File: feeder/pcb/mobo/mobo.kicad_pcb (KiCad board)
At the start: 2 copper layers, 200 x 100 mm, 66 parts, among them J1 FTDI_HEADER, J2 PLATED_PADS, J3 SWD_10, M1 DRIVE_MOTOR, M2 PEEL_MOTOR, SW1 BUTTON_1, SW2 BUTTON_2, SW3 RESET, U1 TCS40DPR, U2 VCNT2020, U3 MAX3078E, U4 DRV8833PWP, U5 AP1117-33, U6 STM32F103C8Tx, U7 MCP16301, U8 QRE1113, Y1 8MHz

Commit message: Fixes #253
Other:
- rule pad_to_mask_clearance: 0.04 -> 0

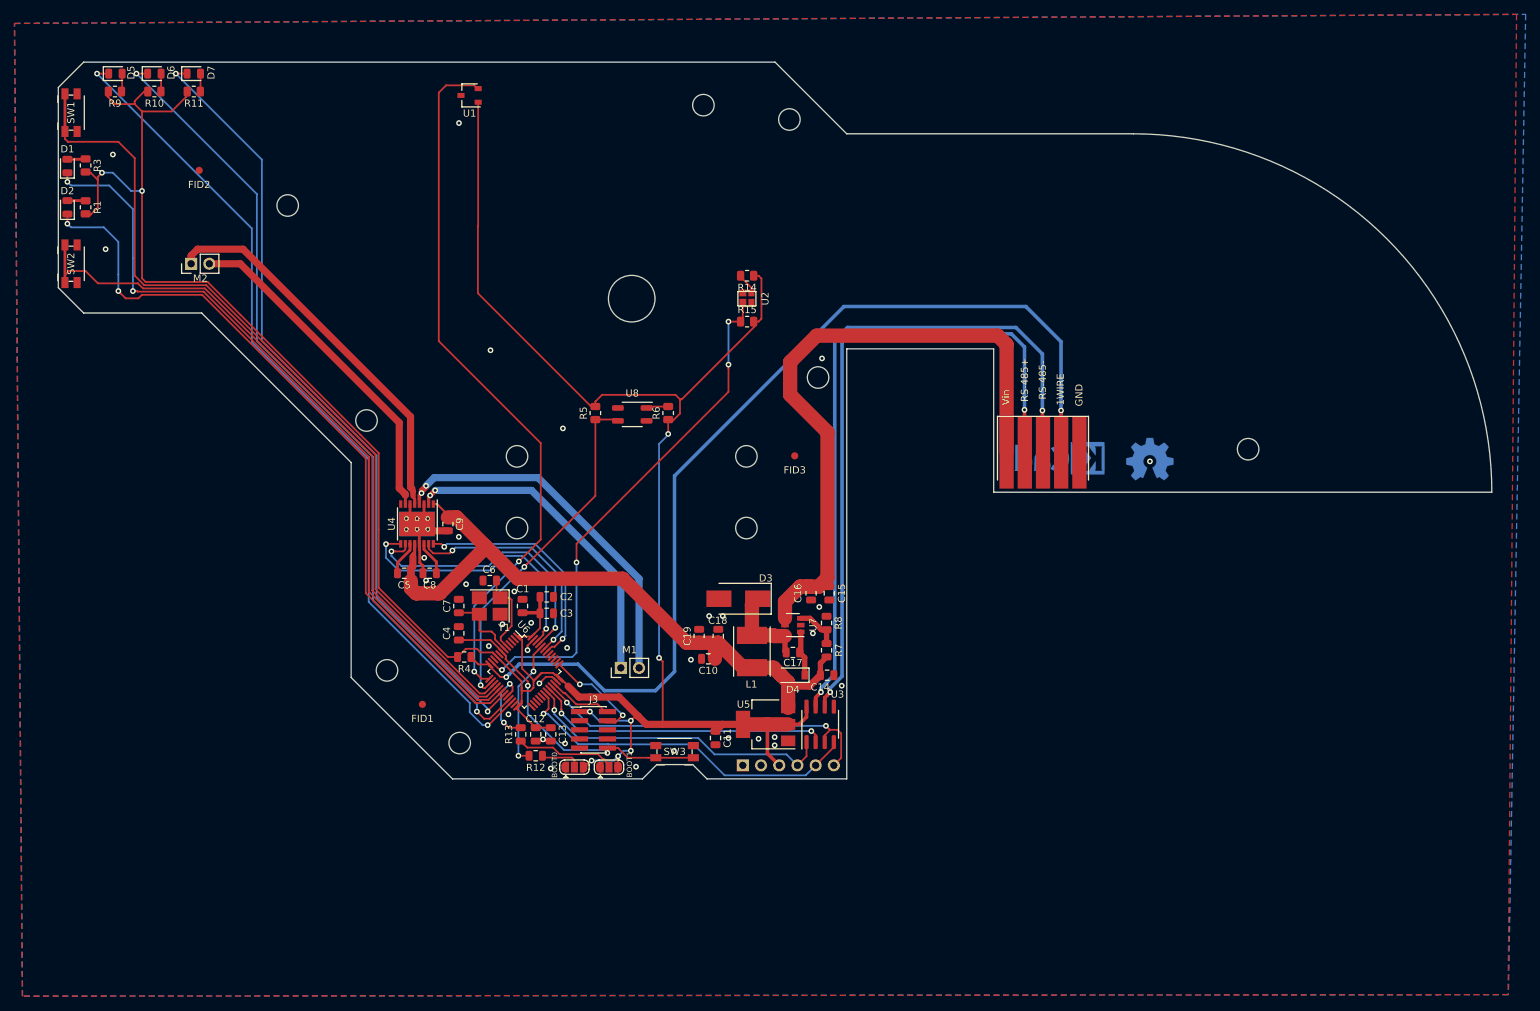
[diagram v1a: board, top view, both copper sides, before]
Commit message: Cleanup Feeders and beautify them
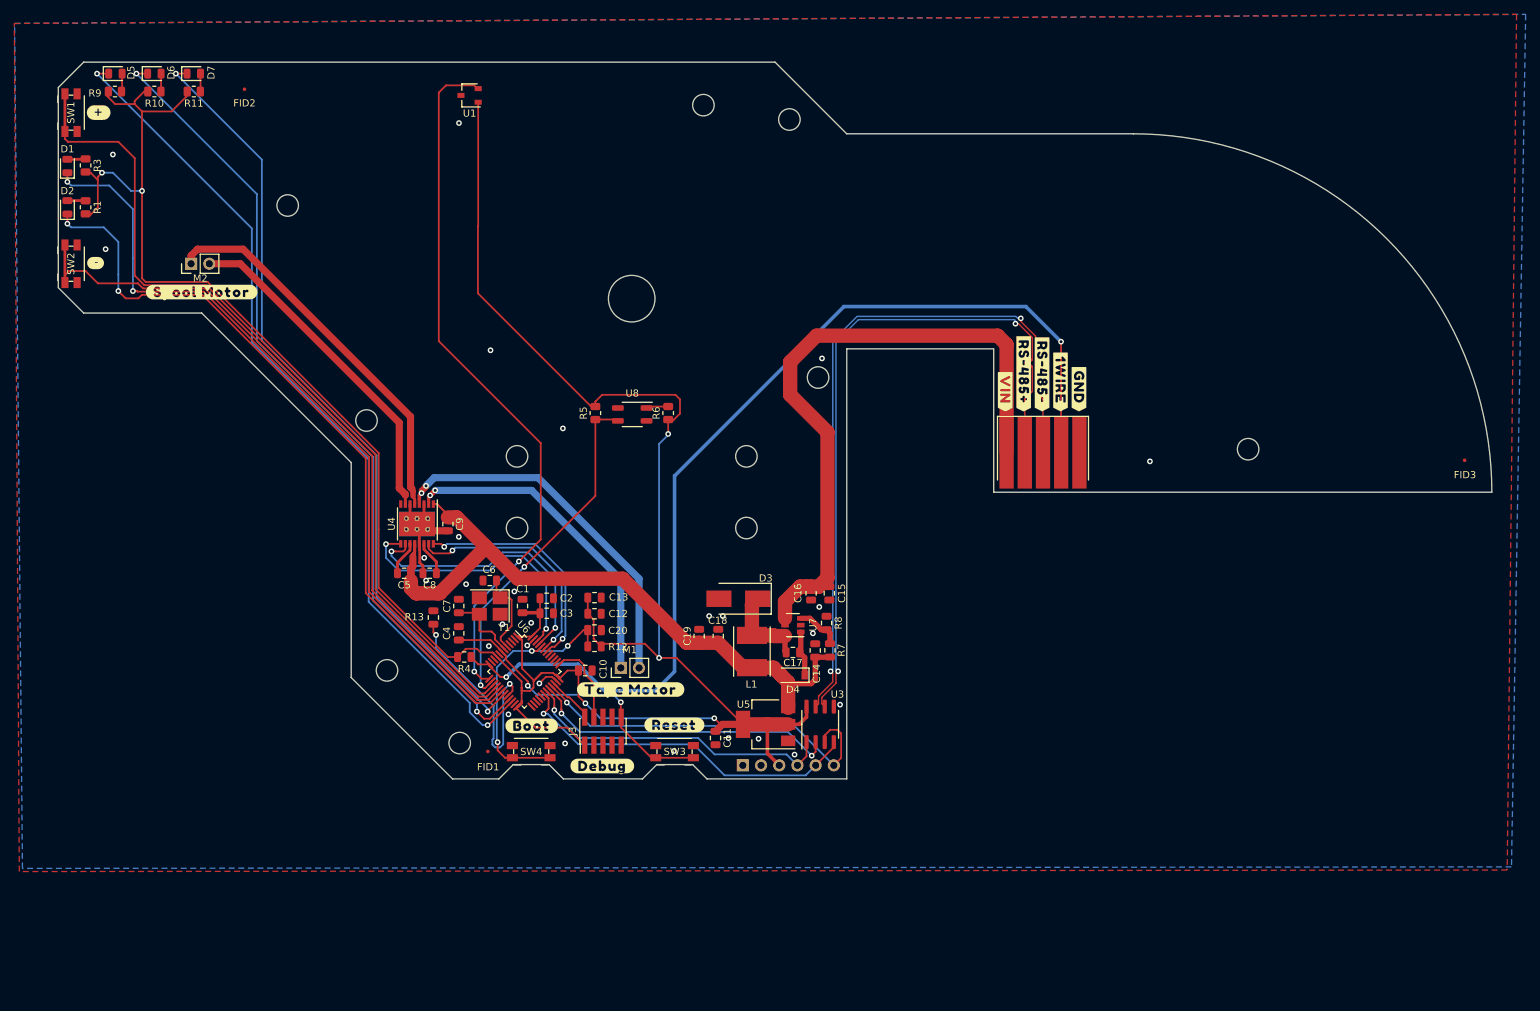
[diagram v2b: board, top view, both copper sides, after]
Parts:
- removed JP2, JP3: SolderJumper_3_Open, Jumper:SolderJumper-3_P1.3mm_Open_RoundedPad1.0x1.5mm
- removed R14: 470R, Resistor_SMD:R_0805_2012Metric
- removed R15: 10K, Resistor_SMD:R_0805_2012Metric
- removed REF**: OSHW-Symbol_6.7x6mm_Copper, Symbol:OSHW-Symbol_6.7x6mm_Copper
- removed REF**: KiCad-Logo_5mm_Copper, Symbol:KiCad-Logo_5mm_Copper
- removed U2: VCNT2020, index:VCNT2020
- added ?: , buzzard_labels, B.Cu at (8.57, 12.4)
- added ?: , buzzard_labels, B.Cu at (184.2, 57.6)
- added ?: , buzzard_labels, F.Cu at (148.5, 50.8)
- added ?: , buzzard_labels, F.Cu at (145.9, 49.8)
- added ?: , buzzard_labels, F.Cu at (143.4, 48.7)
- added ?: , buzzard_labels, F.Cu at (140.8, 48.6)
- added ?: , buzzard_labels, F.Cu at (138.2, 51.1)
- added ?: , buzzard_labels, B.Cu at (114.4, 99.0)
- added ?: , buzzard_labels, B.Cu at (111.8, 98.8)
- added ?: , buzzard_labels, B.Cu at (109.2, 98.9)
- added ?: , buzzard_labels, B.Cu at (106.7, 97.8)
- added ?: , buzzard_labels, B.Cu at (7.85, 33.5)
- added ?: , buzzard_labels, B.Cu at (104.1, 98.9)
- added ?: , buzzard_labels, B.Cu at (101.6, 98.1)
- added ?: , buzzard_labels, B.Cu at (92.1, 101.7)
- added ?: , buzzard_labels, B.Cu at (72.1, 101.7)
- added ?: , buzzard_labels, F.Cu at (72.1, 98.0)
- added ?: , buzzard_labels, F.Cu at (92.0, 97.9)
- added ?: , buzzard_labels, F.Cu at (11.3, 33.4)
- added ?: , buzzard_labels, F.Cu at (11.7, 12.4)
- added ?: , buzzard_labels, F.Cu at (26.1, 37.5)
- added ?: , buzzard_labels, F.Cu at (86.0, 92.9)
- added ?: , buzzard_labels, F.Cu at (82.0, 103.6)
- added ?: , buzzard_labels, B.Cu at (107.9, 92.7)
- added ?: , buzzard_labels, B.Cu at (187.1, 60.1)
- added C20: 100nF, Capacitor_SMD:C_0805_2012Metric, F.Cu at (80.9, 84.6)
- added SW4: RESET, Button_Switch_SMD:Panasonic_EVQPUJ_EVQPUA, F.Cu at (72.1, 101.6)
- C1, C17, C3, C4: value 0.1uF -> 100nF
- C10: value 10uF -> 100nF
- C12, C5: value 0.01uF -> 10nF
- C14: value 100uF -> 10uF
- FID1, FID2, FID3: footprint Fiducial:Fiducial_1mm_Mask2mm -> Fiducial:Fiducial_0.5mm_Mask1mm
- R7: value 52.3K -> 56k
- moved FID3 93.5 mm to (202.3, 61.0)
- moved R13 20.4 mm to (58.4, 82.9), turned to 270 degrees
- moved C13 20.0 mm to (80.9, 80.1), turned to 0 degrees
- moved C12 18.7 mm to (80.9, 82.4), turned to 0 degrees
- moved R12 17.3 mm to (80.9, 86.9), turned to 0 degrees
- moved C10 17.2 mm to (79.6, 90.3), turned to 0 degrees
- moved FID2 13.0 mm to (32.1, 9.18)
- moved FID1 11.3 mm to (66.0, 101.6)
- moved C14 3.83 mm to (111.7, 87.5), turned to 90 degrees
- moved G*** 3.58 mm to (195.9, 58.8), turned to 0 degrees
- moved J3 1.33 mm to (82.1, 98.7), turned to 90 degrees
- moved R7 0.47 mm to (113.8, 87.5)
- moved C2 0.19 mm to (74.2, 80.2)
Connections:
- net BOOT1 renamed Net-(R13-Pad2)
- C10 pad 1: +5V -> +3V3
- R12 pad 1: Net-(JP2-Pad2) -> BOOT0
- R12 pad 2: BOOT0 -> +3V3
- R13 pad 1: Net-(JP3-Pad2) -> GND
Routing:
- net OPTO_SIG_VCNT2020: track 72.6 -> 0.00 mm, vias 4 -> 0
- net Net-(R13-Pad2): track 10.9 -> 33.2 mm
- net BOOT0: track 18.0 -> 38.1 mm, vias 2 -> 3
- net Net-(JP3-Pad2): track 14.1 -> 0.00 mm
- net +3V3: track 384.2 -> 370.1 mm, vias 9 -> 6
- net RS-485+: track 94.1 -> 100.7 mm
- net Net-(JP2-Pad2): track 6.20 -> 0.00 mm
- net Net-(R14-Pad2): track 3.07 -> 0.00 mm
- net GND: track 25.8 -> 22.9 mm, vias 34 -> 28
- net SWCLK: track 14.6 -> 11.8 mm, vias 2 -> 0
- net DE: track 50.1 -> 52.6 mm, vias 2 -> 1
- net SWDIO: track 8.75 -> 6.56 mm
- net _RE: track 41.8 -> 43.6 mm
- net RS-485-: track 99.4 -> 100.8 mm
- net +5V: track 100.6 -> 99.1 mm
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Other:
- outline, holes or cut-outs redrawn
- board text added: "<<hash>>"
- board text removed: "1WIRE"
- board text removed: "BOOT0"
- board text removed: "BOOT1"
- board text removed: "GND"
- board text removed: "Index Feeder REV05<<hash>>"
- board text removed: "RS-485+"
- board text removed: "RS-485-"
- board text removed: "Vin"

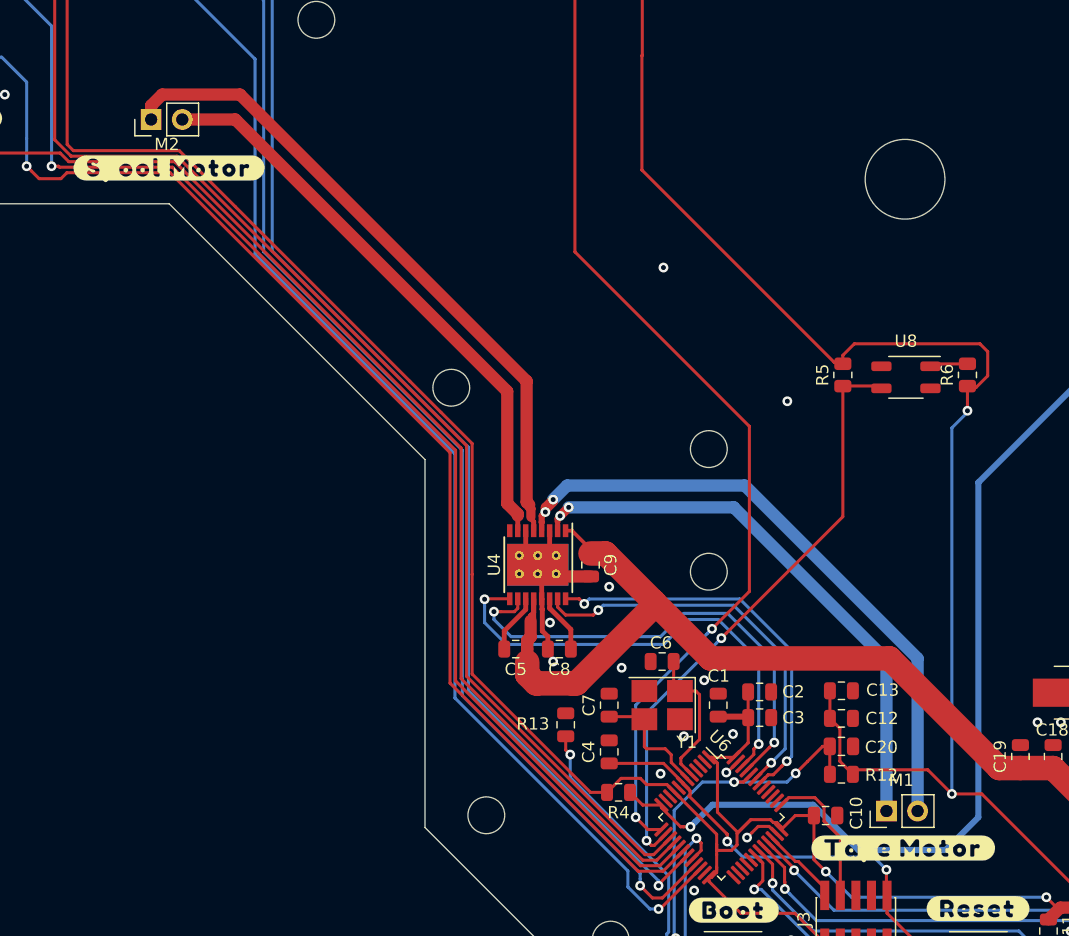
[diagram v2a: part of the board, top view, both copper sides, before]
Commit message: Avoid using the letter p for labels
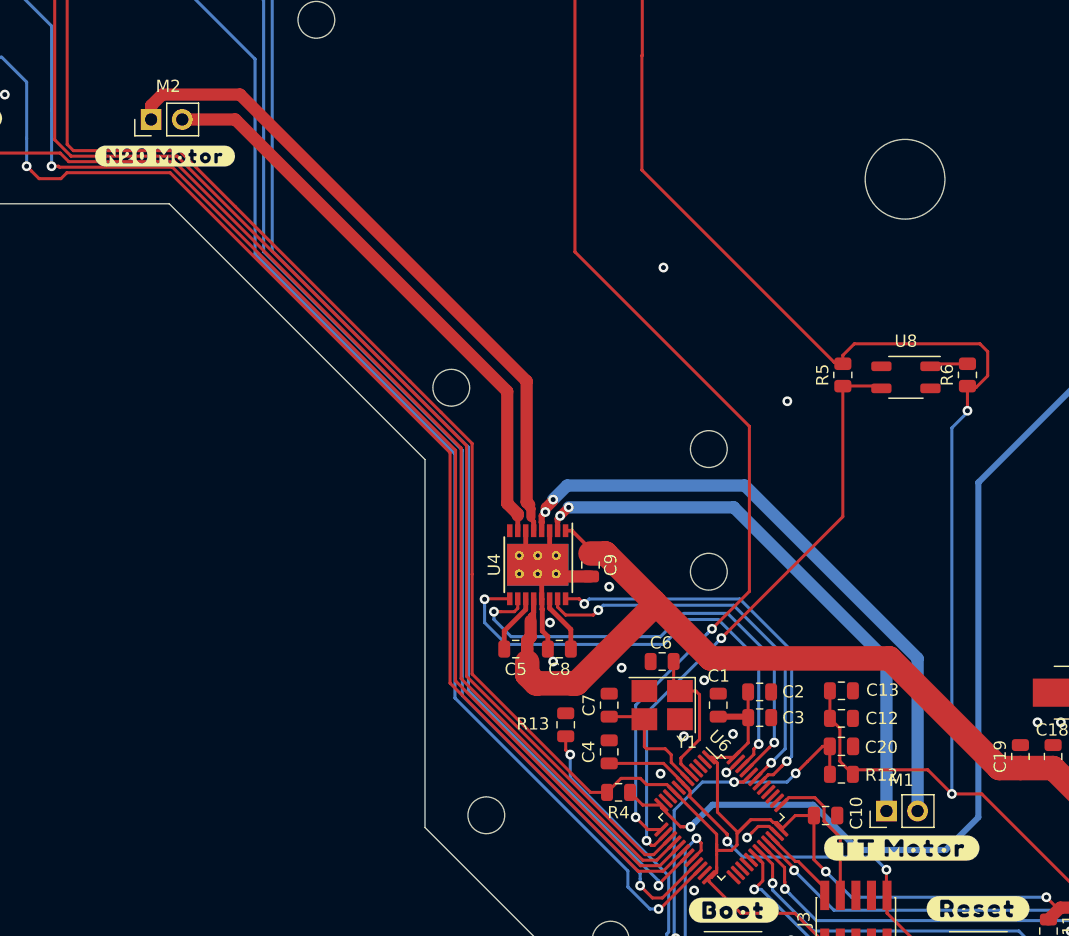
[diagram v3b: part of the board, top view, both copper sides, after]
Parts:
- removed the ? at (26.1, 37.5)
- removed the ? at (86.0, 92.9)
- added ?: , buzzard_labels, F.Cu at (25.8, 36.5)
- added ?: , buzzard_labels, F.Cu at (85.8, 92.9)

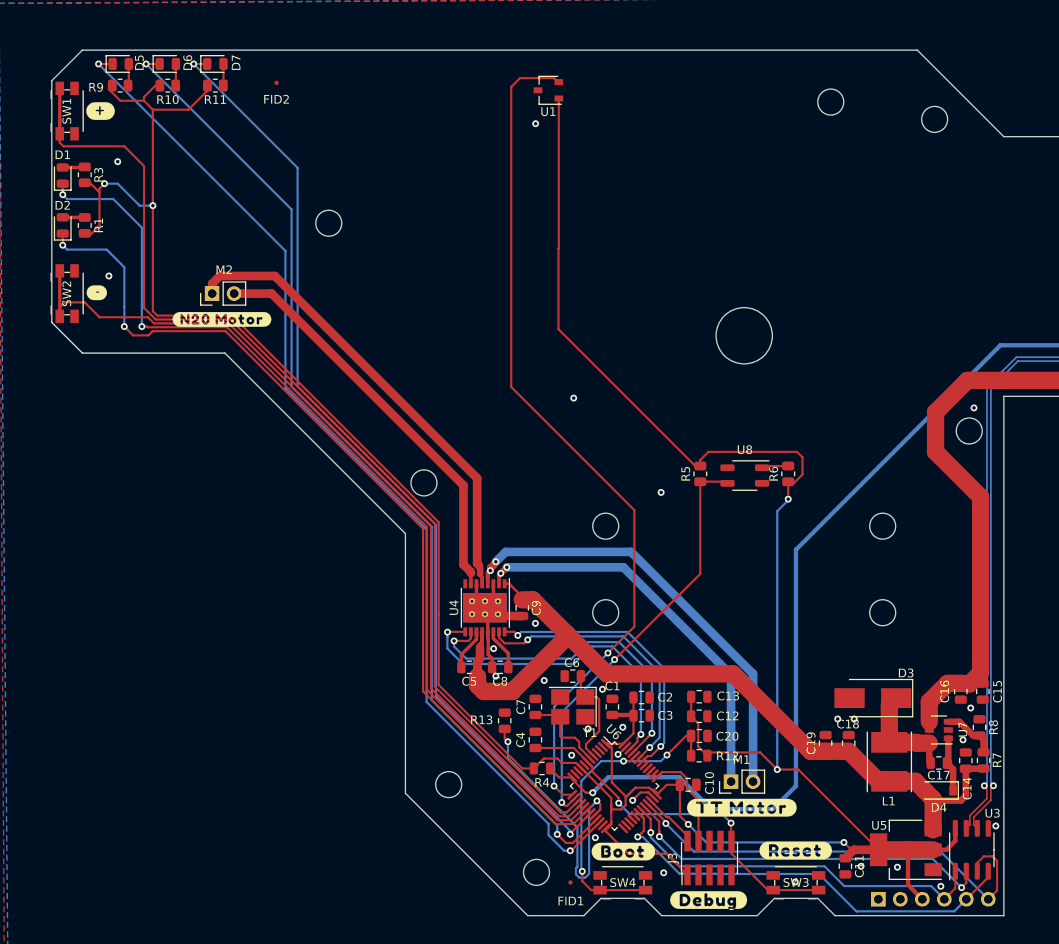
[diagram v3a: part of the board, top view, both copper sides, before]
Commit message: Fix reset logic level
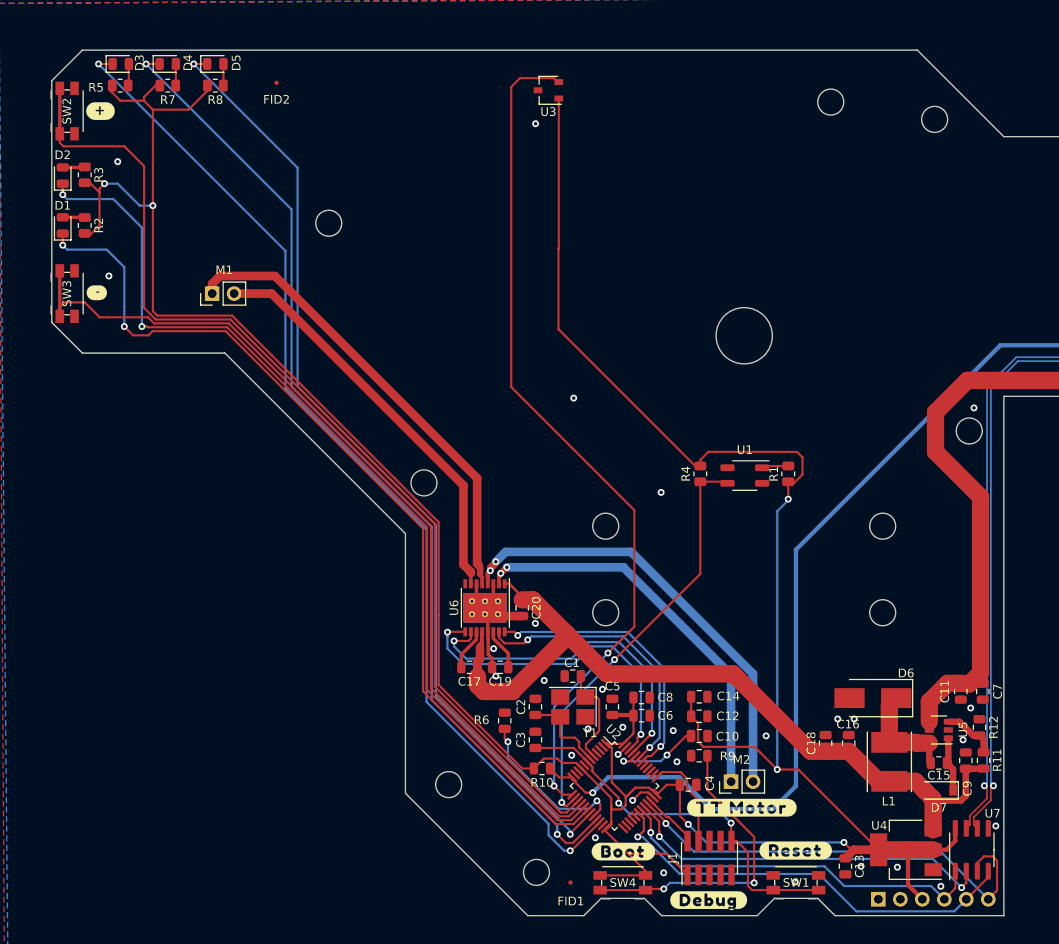
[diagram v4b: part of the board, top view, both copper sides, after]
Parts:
- removed the ? at (25.8, 36.5)
- SW4: value RESET -> BOOT
- renumbered C6 to C1, C20 to C10, C16 to C11, C11 to C13, C13 to C14, C17 to C15, C18 to C16, C5 to C17, C19 to C18, C8 to C19, C7 to C2, C9 to C20, C4 to C3, C10 to C4, C1 to C5, C3 to C6, C15 to C7, C2 to C8, C14 to C9, D2 to D1, D1 to D2, D5 to D3, D6 to D4, D7 to D5, D3 to D6, D4 to D7, J3 to J1, J1 to J2, J2 to J3, M2 to M1, M1 to M2, R6 to R1, R4 to R10, R7 to R11, R8 to R12, R1 to R2, R5 to R4, R9 to R5, R13 to R6, R10 to R7, R11 to R8, R12 to R9, SW3 to SW1, SW1 to SW2, SW2 to SW3, U8 to U1, U6 to U2, U1 to U3, U5 to U4, U7 to U5, U4 to U6, U3 to U7
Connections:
- R9 pad 1: BOOT0 -> GND
- R9 pad 2: +3V3 -> Net-(R9-Pad2)
- SW4 pad 1: BOOT0 -> Net-(R9-Pad2)
- SW4 pad 2: GND -> +3V3
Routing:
- net Net-(R9-Pad2): track 0.00 -> 35.6 mm, vias 0 -> 2
- net BOOT0: track 38.1 -> 10.6 mm, vias 3 -> 2
- net Net-(R6-Pad2): track 33.2 -> 20.1 mm
- net +3V3: track 370.1 -> 378.0 mm
- net RESET: track 42.3 -> 43.8 mm
- net GND: vias 28 -> 31
